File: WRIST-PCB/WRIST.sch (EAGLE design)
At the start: 44 parts, among them Q3 BSS138, U3 LP5907-2.8V

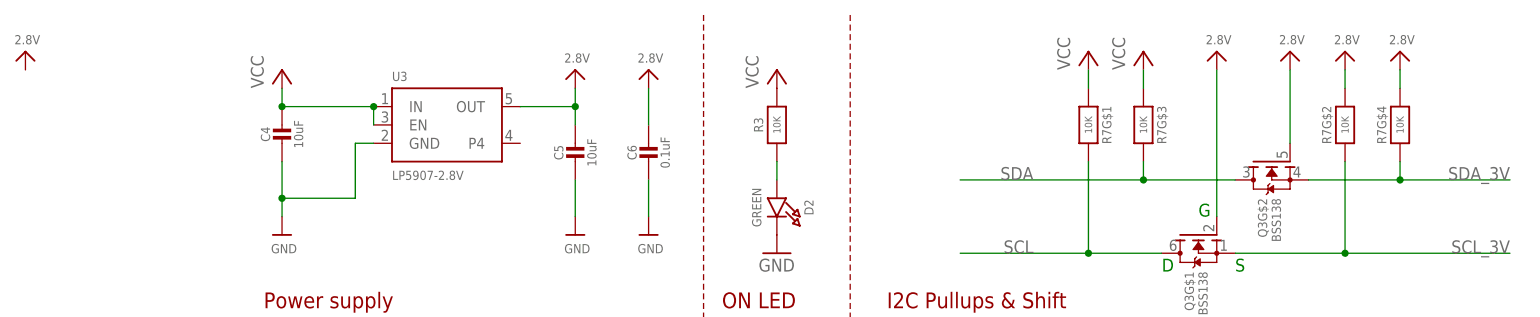
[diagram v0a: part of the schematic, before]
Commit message: update pcb through holes and design
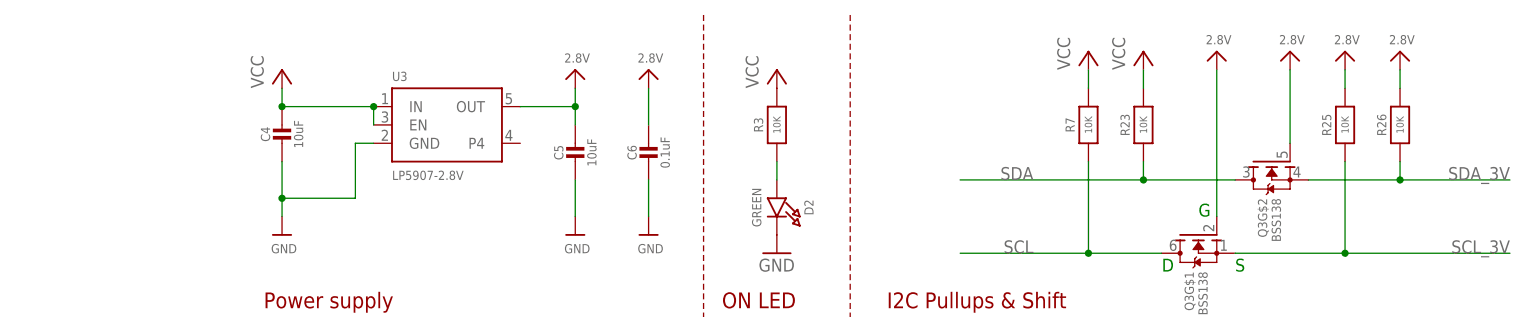
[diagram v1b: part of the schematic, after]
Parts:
- added R23, R25, R26: 10K, microbuilder:RESISTOR_0603_NOOUT
- R7: device microbuilder:RESISTOR_4PACK -> microbuilder:RESISTOR_0603_NOOUT
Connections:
- net 2.8V: now also R25.2, R26.2; no longer R7G$2.1, R7G$4.1
- net SCL: now also R7.1; no longer R7G$1.2
- net SCL_3V: now also R25.1; no longer R7G$2.2
- net SDA: now also R23.1; no longer R7G$3.2
- net SDA_3V: now also R26.1; no longer R7G$4.2
- net VCC: now also R23.2, R7.2; no longer R7G$1.1, R7G$3.1
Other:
- moved on the sheet: R7
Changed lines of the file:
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@@
 <part name="C6" library="microbuilder" deviceset="CAP_CERAMIC" device="0603_NO" value="0.1uF"/>
 <part name="U$22" library="microbuilder" deviceset="GND" device=""/>
-<part name="R7" library="microbuilder" deviceset="RESISTOR_4PACK" device="" value="10K"/>
 <part name="Q3" library="microbuilder" deviceset="MOSFET-N_DUAL" device="" value="BSS138"/>
 <part name="U$32" library="microbuilder" deviceset="FRAME_A4_ADAFRUIT" device=""/>
@@
 <part name="U$3" library="microbuilder" deviceset="GND" device=""/>
 <part name="J5" library="SparkFun-Connectors" library_urn="urn:adsk.eagle:library:513" deviceset="CONN_02" device="1X02_NO_SILK" package3d_urn="urn:adsk.eagle:package:38051/1"/>
-<part name="U$4" library="microbuilder" deviceset="2.8V" device=""/>
 <part name="U$5" library="microbuilder" deviceset="2.8V" device=""/>
 <part name="J6" library="SparkFun-Connectors" library_urn="urn:adsk.eagle:library:513" deviceset="CONN_02" device="1X02_NO_SILK" package3d_urn="urn:adsk.eagle:package:38051/1"/>
@@
 <part name="R21" library="microbuilder" deviceset="RESISTOR" device="_0603_NOOUT" value="10K"/>
 <part name="R22" library="microbuilder" deviceset="RESISTOR" device="_0603_NOOUT" value="10K"/>
+<part name="R7" library="microbuilder" deviceset="RESISTOR" device="_0603_NOOUT" value="10K"/>
+<part name="R23" library="microbuilder" deviceset="RESISTOR" device="_0603_NOOUT" value="10K"/>
+<part name="R25" library="microbuilder" deviceset="RESISTOR" device="_0603_NOOUT" value="10K"/>
+<part name="R26" library="microbuilder" deviceset="RESISTOR" device="_0603_NOOUT" value="10K"/>
 </parts>
 <sheets>
@@
 <attribute name="VALUE" x="209.296" y="154.94" size="1.27" layer="96"/>
 </instance>
-<instance part="R7" gate="G$4" x="165.1" y="160.02" smashed="yes" rot="MR270">
-<attribute name="NAME" x="162.56" y="160.02" size="1.27" layer="95" font="vector" rot="MR270" align="center"/>
-<attribute name="VALUE" x="165.1" y="160.02" size="1.016" layer="96" font="vector" ratio="15" rot="MR270" align="center"/>
-</instance>
-<instance part="R7" gate="G$2" x="157.48" y="160.02" smashed="yes" rot="MR270">
-<attribute name="NAME" x="154.94" y="160.02" size="1.27" layer="95" font="vector" rot="MR270" align="center"/>
-<attribute name="VALUE" x="157.48" y="160.02" size="1.016" layer="96" font="vector" ratio="15" rot="MR270" align="center"/>
-</instance>
 <instance part="Q3" gate="G$1" x="137.16" y="144.78" smashed="yes" rot="MR270">
 <attribute name="NAME" x="136.525" y="139.7" size="1.27" layer="95" rot="MR270"/>
@@
 <attribute name="VALUE" x="148.59" y="149.86" size="1.27" layer="96" rot="MR270"/>
 </instance>
-<instance part="R7" gate="G$3" x="129.54" y="160.02" smashed="yes" rot="R270">
-<attribute name="NAME" x="132.08" y="160.02" size="1.27" layer="95" font="vector" rot="R270" align="center"/>
-<attribute name="VALUE" x="129.54" y="160.02" size="1.016" layer="96" font="vector" ratio="15" rot="R270" align="center"/>
-</instance>
-<instance part="R7" gate="G$1" x="121.92" y="160.02" smashed="yes" rot="R270">
-<attribute name="NAME" x="124.46" y="160.02" size="1.27" layer="95" font="vector" rot="R270" align="center"/>
-<attribute name="VALUE" x="121.92" y="160.02" size="1.016" layer="96" font="vector" ratio="15" rot="R270" align="center"/>
-</instance>
 <instance part="P+1" gate="VCC" x="121.92" y="170.18" smashed="yes">
 <attribute name="VALUE" x="119.38" y="167.64" size="1.778" layer="96" rot="R90"/>
@@
 <attribute name="NAME" x="220.98" y="168.148" size="1.778" layer="95" font="vector"/>
 </instance>
-<instance part="U$4" gate="G$1" x="-25.4" y="170.18" smashed="yes">
-<attribute name="VALUE" x="-26.924" y="171.196" size="1.27" layer="96"/>
-</instance>
 <instance part="U$5" gate="G$1" x="236.22" y="167.64" smashed="yes">
 <attribute name="VALUE" x="234.696" y="168.656" size="1.27" layer="96"/>
@@
 <attribute name="NAME" x="152.4" y="81.28" size="1.27" layer="95" font="vector" rot="R90" align="center"/>
 <attribute name="VALUE" x="154.94" y="81.28" size="1.016" layer="96" font="vector" ratio="15" rot="R90" align="center"/>
+</instance>
+<instance part="R7" gate="G$1" x="121.92" y="160.02" smashed="yes" rot="R90">
+<attribute name="NAME" x="119.38" y="160.02" size="1.27" layer="95" font="vector" rot="R90" align="center"/>
+<attribute name="VALUE" x="121.92" y="160.02" size="1.016" layer="96" font="vector" ratio="15" rot="R90" align="center"/>
+</instance>
+<instance part="R23" gate="G$1" x="129.54" y="160.02" smashed="yes" rot="R90">
+<attribute name="NAME" x="127" y="160.02" size="1.27" layer="95" font="vector" rot="R90" align="center"/>
+<attribute name="VALUE" x="129.54" y="160.02" size="1.016" layer="96" font="vector" ratio="15" rot="R90" align="center"/>
+</instance>
+<instance part="R25" gate="G$1" x="157.48" y="160.02" smashed="yes" rot="R90">
+<attribute name="NAME" x="154.94" y="160.02" size="1.27" layer="95" font="vector" rot="R90" align="center"/>
+<attribute name="VALUE" x="157.48" y="160.02" size="1.016" layer="96" font="vector" ratio="15" rot="R90" align="center"/>
+</instance>
+<instance part="R26" gate="G$1" x="165.1" y="160.02" smashed="yes" rot="R90">
+<attribute name="NAME" x="162.56" y="160.02" size="1.27" layer="95" font="vector" rot="R90" align="center"/>
+<attribute name="VALUE" x="165.1" y="160.02" size="1.016" layer="96" font="vector" ratio="15" rot="R90" align="center"/>
 </instance>
 </instances>
@@
 <label x="114.3" y="142.24" size="1.778" layer="95" rot="MR0"/>
 <pinref part="Q3" gate="G$1" pin="D"/>
-<pinref part="R7" gate="G$1" pin="2"/>
 <wire x1="121.92" y1="142.24" x2="104.14" y2="142.24" width="0.1524" layer="91"/>
 <wire x1="121.92" y1="154.94" x2="121.92" y2="142.24" width="0.1524" layer="91"/>
 <junction x="121.92" y="142.24"/>
+<pinref part="R7" gate="G$1" pin="1"/>
 </segment>
 <segment>
@@
 <label x="114.3" y="152.4" size="1.778" layer="95" rot="MR0"/>
 <pinref part="Q3" gate="G$2" pin="D"/>
-<pinref part="R7" gate="G$3" pin="2"/>
 <wire x1="129.54" y1="152.4" x2="104.14" y2="152.4" width="0.1524" layer="91"/>
 <wire x1="129.54" y1="154.94" x2="129.54" y2="152.4" width="0.1524" layer="91"/>
 <junction x="129.54" y="152.4"/>
+<pinref part="R23" gate="G$1" pin="1"/>
 </segment>
 <segment>
@@
 <net name="VCC" class="1">
 <segment>
-<pinref part="R7" gate="G$1" pin="1"/>
 <wire x1="121.92" y1="167.64" x2="121.92" y2="165.1" width="0.1524" layer="91"/>
 <pinref part="P+1" gate="VCC" pin="VCC"/>
-</segment>
-<segment>
-<pinref part="R7" gate="G$3" pin="1"/>
+<pinref part="R7" gate="G$1" pin="2"/>
+</segment>
+<segment>
 <wire x1="129.54" y1="165.1" x2="129.54" y2="167.64" width="0.1524" layer="91"/>
 <pinref part="P+2" gate="VCC" pin="VCC"/>
+<pinref part="R23" gate="G$1" pin="2"/>
 </segment>
 <segment>
@@
 <wire x1="157.48" y1="154.94" x2="157.48" y2="142.24" width="0.1524" layer="91"/>
 <junction x="157.48" y="142.24"/>
-<pinref part="R7" gate="G$2" pin="2"/>
 <pinref part="Q3" gate="G$1" pin="S"/>
+<pinref part="R25" gate="G$1" pin="1"/>
 </segment>
 <segment>
@@
 <wire x1="165.1" y1="154.94" x2="165.1" y2="152.4" width="0.1524" layer="91"/>
 <junction x="165.1" y="152.4"/>
-<pinref part="R7" gate="G$4" pin="2"/>
 <pinref part="Q3" gate="G$2" pin="S"/>
+<pinref part="R26" gate="G$1" pin="1"/>
 </segment>
 <segment>
@@
 </segment>
 <segment>
-<wire x1="149.86" y1="157.48" x2="149.86" y2="167.64" width="0.1524" layer="91"/>
-<pinref part="Q3" gate="G$2" pin="G"/>
-<pinref part="U$25" gate="G$1" pin="2.8V"/>
-</segment>
-<segment>
 <wire x1="157.48" y1="165.1" x2="157.48" y2="167.64" width="0.1524" layer="91"/>
-<pinref part="R7" gate="G$2" pin="1"/>
 <pinref part="U$26" gate="G$1" pin="2.8V"/>
+<pinref part="R25" gate="G$1" pin="2"/>
 </segment>
 <segment>
 <wire x1="165.1" y1="165.1" x2="165.1" y2="167.64" width="0.1524" layer="91"/>
-<pinref part="R7" gate="G$4" pin="1"/>
 <pinref part="U$27" gate="G$1" pin="2.8V"/>
+<pinref part="R26" gate="G$1" pin="2"/>
 </segment>
 <segment>
@@
 <pinref part="R21" gate="G$1" pin="2"/>
 </segment>
-</net>
+<segment>
+<pinref part="Q3" gate="G$2" pin="G"/>
+<pinref part="U$25" gate="G$1" pin="2.8V"/>
+<wire x1="149.86" y1="157.48" x2="149.86" y2="167.64" width="0.1524" layer="91"/>
+</segment>
+</net>

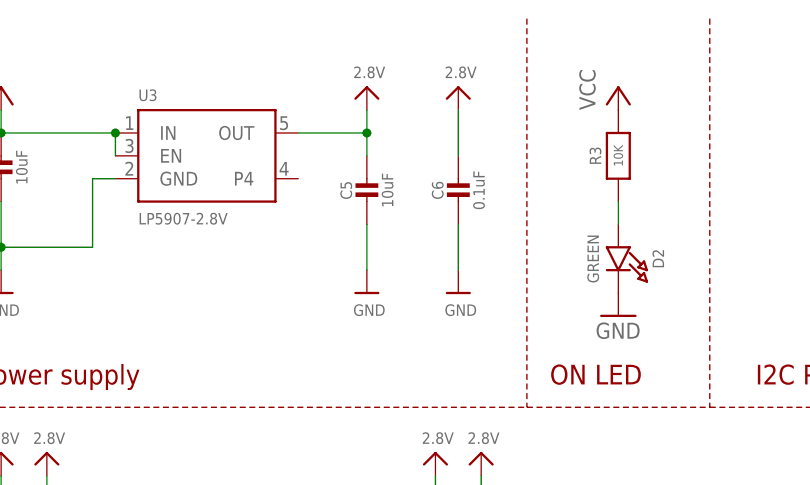
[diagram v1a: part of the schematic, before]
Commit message: replace smt capacitor with holes
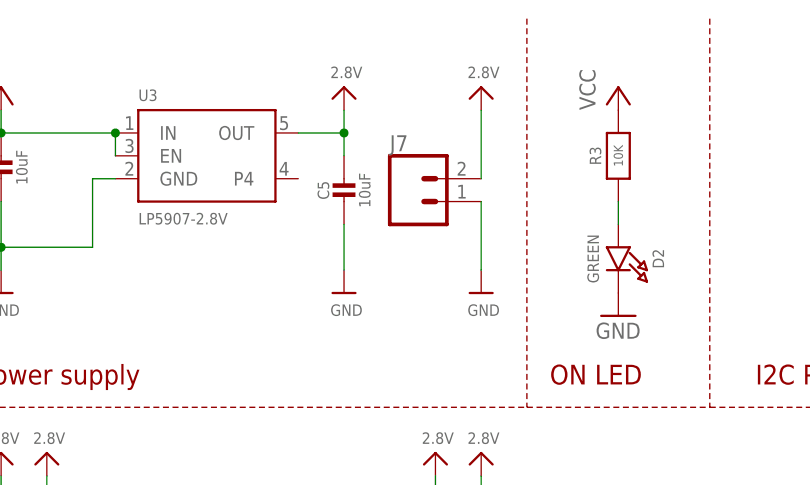
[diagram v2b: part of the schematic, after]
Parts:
- removed C6: 0.1uF, microbuilder:CAP_CERAMIC0603_NO
- added J7: (no value), SparkFun-Connectors:CONN_021X02_NO_SILK
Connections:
- net 2.8V: now also J7.2; no longer C6.1
- net GND: now also J7.1; no longer C6.2
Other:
- moved on the sheet: C5
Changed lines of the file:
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@@
 <part name="U$20" library="microbuilder" deviceset="GND" device=""/>
 <part name="U$21" library="microbuilder" deviceset="GND" device=""/>
-<part name="C6" library="microbuilder" deviceset="CAP_CERAMIC" device="0603_NO" value="0.1uF"/>
 <part name="U$22" library="microbuilder" deviceset="GND" device=""/>
 <part name="Q3" library="microbuilder" deviceset="MOSFET-N_DUAL" device="" value="BSS138"/>
@@
 <part name="R25" library="microbuilder" deviceset="RESISTOR" device="_0603_NOOUT" value="10K"/>
 <part name="R26" library="microbuilder" deviceset="RESISTOR" device="_0603_NOOUT" value="10K"/>
+<part name="J7" library="SparkFun-Connectors" library_urn="urn:adsk.eagle:library:513" deviceset="CONN_02" device="1X02_NO_SILK" package3d_urn="urn:adsk.eagle:package:38051/1"/>
 </parts>
 <sheets>
@@
 <attribute name="VALUE" x="25.4" y="152.4" size="1.27" layer="95"/>
 </instance>
-<instance part="C5" gate="G$1" x="50.8" y="154.94" smashed="yes">
-<attribute name="NAME" x="48.51" y="156.19" size="1.27" layer="95" font="vector" rot="R90" align="center"/>
-<attribute name="VALUE" x="53.1" y="156.19" size="1.27" layer="96" font="vector" rot="R90" align="center"/>
-</instance>
-<instance part="U$20" gate="G$1" x="50.8" y="144.78" smashed="yes">
-<attribute name="VALUE" x="49.276" y="142.24" size="1.27" layer="96"/>
-</instance>
-<instance part="U$21" gate="G$1" x="60.96" y="144.78" smashed="yes">
-<attribute name="VALUE" x="59.436" y="142.24" size="1.27" layer="96"/>
-</instance>
-<instance part="C6" gate="G$1" x="60.96" y="154.94" smashed="yes">
-<attribute name="NAME" x="58.67" y="156.19" size="1.27" layer="95" font="vector" rot="R90" align="center"/>
-<attribute name="VALUE" x="63.26" y="156.19" size="1.27" layer="96" font="vector" rot="R90" align="center"/>
+<instance part="C5" gate="G$1" x="48.26" y="154.94" smashed="yes">
+<attribute name="NAME" x="45.97" y="156.19" size="1.27" layer="95" font="vector" rot="R90" align="center"/>
+<attribute name="VALUE" x="50.56" y="156.19" size="1.27" layer="96" font="vector" rot="R90" align="center"/>
+</instance>
+<instance part="U$20" gate="G$1" x="48.26" y="144.78" smashed="yes">
+<attribute name="VALUE" x="46.736" y="142.24" size="1.27" layer="96"/>
+</instance>
+<instance part="U$21" gate="G$1" x="63.5" y="144.78" smashed="yes">
+<attribute name="VALUE" x="61.976" y="142.24" size="1.27" layer="96"/>
 </instance>
 <instance part="U$22" gate="G$1" x="210.82" y="157.48" smashed="yes">
@@
 <attribute name="VALUE" x="208.28" y="165.1" size="1.778" layer="96" rot="R90"/>
 </instance>
-<instance part="U$40" gate="G$1" x="60.96" y="167.64" smashed="yes">
-<attribute name="VALUE" x="59.436" y="168.656" size="1.27" layer="96"/>
-</instance>
-<instance part="U$23" gate="G$1" x="50.8" y="167.64" smashed="yes">
-<attribute name="VALUE" x="49.276" y="168.656" size="1.27" layer="96"/>
+<instance part="U$40" gate="G$1" x="63.5" y="167.64" smashed="yes">
+<attribute name="VALUE" x="61.976" y="168.656" size="1.27" layer="96"/>
+</instance>
+<instance part="U$23" gate="G$1" x="48.26" y="167.64" smashed="yes">
+<attribute name="VALUE" x="46.736" y="168.656" size="1.27" layer="96"/>
 </instance>
 <instance part="P+5" gate="VCC" x="78.74" y="167.64" smashed="yes">
@@
 <attribute name="NAME" x="162.56" y="160.02" size="1.27" layer="95" font="vector" rot="R90" align="center"/>
 <attribute name="VALUE" x="165.1" y="160.02" size="1.016" layer="96" font="vector" ratio="15" rot="R90" align="center"/>
+</instance>
+<instance part="J7" gate="G$1" x="55.88" y="154.94" smashed="yes">
+<attribute name="VALUE" x="53.34" y="150.114" size="1.778" layer="96" font="vector"/>
+<attribute name="NAME" x="53.34" y="160.528" size="1.778" layer="95" font="vector"/>
 </instance>
 </instances>
@@
 <pinref part="C5" gate="G$1" pin="2"/>
 <pinref part="U$20" gate="G$1" pin="GND"/>
-<wire x1="50.8" y1="152.4" x2="50.8" y2="147.32" width="0.1524" layer="91"/>
+<wire x1="48.26" y1="152.4" x2="48.26" y2="147.32" width="0.1524" layer="91"/>
 </segment>
 <segment>
 <pinref part="U$21" gate="G$1" pin="GND"/>
-<pinref part="C6" gate="G$1" pin="2"/>
-<wire x1="60.96" y1="152.4" x2="60.96" y2="147.32" width="0.1524" layer="91"/>
+<wire x1="63.5" y1="154.94" x2="63.5" y2="147.32" width="0.1524" layer="91"/>
+<pinref part="J7" gate="G$1" pin="1"/>
 </segment>
 <segment>
@@
 <net name="2.8V" class="0">
 <segment>
-<pinref part="C6" gate="G$1" pin="1"/>
-<wire x1="60.96" y1="165.1" x2="60.96" y2="160.02" width="0.1524" layer="91"/>
+<wire x1="63.5" y1="165.1" x2="63.5" y2="157.48" width="0.1524" layer="91"/>
 <pinref part="U$40" gate="G$1" pin="2.8V"/>
-</segment>
-<segment>
-<wire x1="43.18" y1="162.56" x2="50.8" y2="162.56" width="0.1524" layer="91"/>
-<wire x1="50.8" y1="162.56" x2="50.8" y2="165.1" width="0.1524" layer="91"/>
+<pinref part="J7" gate="G$1" pin="2"/>
+</segment>
+<segment>
+<wire x1="43.18" y1="162.56" x2="48.26" y2="162.56" width="0.1524" layer="91"/>
+<wire x1="48.26" y1="162.56" x2="48.26" y2="165.1" width="0.1524" layer="91"/>
 <pinref part="U3" gate="G$1" pin="OUT"/>
 <pinref part="C5" gate="G$1" pin="1"/>
-<wire x1="50.8" y1="162.56" x2="50.8" y2="160.02" width="0.1524" layer="91"/>
-<junction x="50.8" y="162.56"/>
+<wire x1="48.26" y1="162.56" x2="48.26" y2="160.02" width="0.1524" layer="91"/>
+<junction x="48.26" y="162.56"/>
 <pinref part="U$23" gate="G$1" pin="2.8V"/>
 </segment>
